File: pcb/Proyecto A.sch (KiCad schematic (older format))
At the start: 187 parts, among them J1 j, K1 1, K10 10, K11 k, K2 2, K3 3, K4 4, K6 6, K7 7, K8 8, K9 9, M1 KEYSW, P1 p, Q1 q, SW1 SW_Push, T1 t, U1 ATmega32U4-AU, U2 u, X1 x, Y1 16MHZ, Y2 y, k5 5

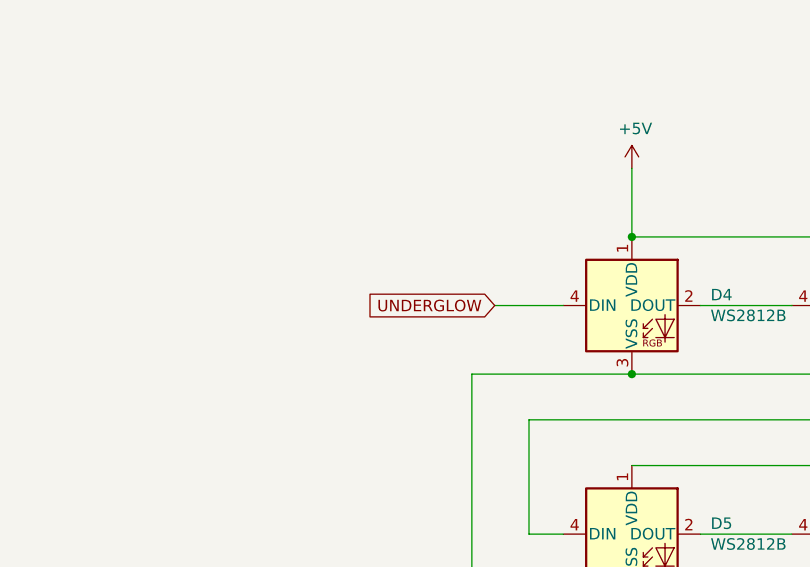
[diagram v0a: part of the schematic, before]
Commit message: added a 500 ohm resistor bettween mcu underglow pin and 1st ws2812b
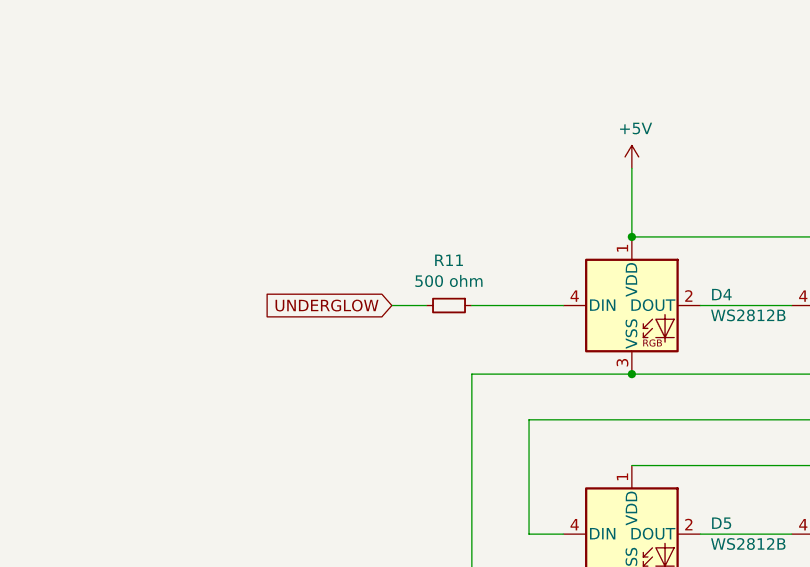
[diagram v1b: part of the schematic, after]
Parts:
- added R11: 500 ohm, Resistor_SMD:R_0805_2012Metric_Pad1.15x1.40mm_HandSolder, symbol Device:R_Small
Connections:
- net UNDERGLOW: now also R11.2; no longer D4.4 (DIN)
- new net: D4.4 (DIN), R11.1
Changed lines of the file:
@@
 Wire Wire Line
 	18600 8750 19000 8750
-Text GLabel 13700 7750 0    50   Input ~ 0
+Text GLabel 13250 7750 0    50   Input ~ 0
 UNDERGLOW
-Wire Wire Line
-	13700 7750 14000 7750
 NoConn ~ 19600 8750
 $Comp
@@
 Connection ~ 17300 11250
 Connection ~ 16350 10850
+$Comp
+L Device:R_Small R11
+U 1 1 5F167937
+P 13500 7750
+F 0 "R11" V 13304 7750 50  0000 C CNN
+F 1 "500 ohm" V 13395 7750 50  0000 C CNN
+F 2 "Resistor_SMD:R_0805_2012Metric_Pad1.15x1.40mm_HandSolder" H 13500 7750 50  0001 C CNN
+F 3 "~" H 13500 7750 50  0001 C CNN
+	1    13500 7750
+	0    1    1    0
+$EndComp
+Wire Wire Line
+	13250 7750 13400 7750
+Wire Wire Line
+	13600 7750 14000 7750
 $EndSCHEMATC

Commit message: Proto 1.1
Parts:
- '1, ,<1, .>1, /1, ;1, =+1, A1, ALT1, B1, B2, BACKSPACE1, C8, CAPS1, CAPS2, CTRL1, D18, E1, Esc1, F2, FUNC1, FUNC2, FUNCT1, G1, H1, I1, J1, K1, K10, K11, K2, K3, K4, K6, K7, K8, K9, KK0, K\1, K_14, L1, M1, N1, O1, P1, PGDN1, PGUP1, Q1, R10, RALT1, RCTL1, RETURN1, RSHIFT1, RSHIFT2, S1, SHIFT1, SPCE2, SPLIT_BKS1, T1, TAB1, U2, V1, W1, X1, Y2, Z1, [1, ]1, _-1, k5, lgui1, space2: symbol MX_Alps_Hybrid:MX-NoLED -> Proyecto-A-rescue:MX-NoLED-MX_Alps_Hybrid
- C1, C10, C11, C12, C13, C14, C15, C16, C17, C18, C19, C2, C20, C21, C3, C4, C5, C6, C9: footprint Capacitor_SMD:C_0805_2012Metric -> Capacitor_SMD:C_0805_2012Metric_Pad1.15x1.40mm_HandSolder
- C7: value 100uf -> 10uf; footprint Capacitor_SMD:C_0805_2012Metric -> Capacitor_SMD:C_0805_2012Metric_Pad1.15x1.40mm_HandSolder
- USB1: footprint Type-C:HRO-TYPE-C-31-M-12-jlc -> Type-C:HRO-TYPE-C-31-M-12-HandSoldering; symbol Type-C:HRO-TYPE-C-31-M-12 -> Proyecto-A-rescue:HRO-TYPE-C-31-M-12-Type-C
- Y1: footprint Crystal:Crystal_SMD_3225-4Pin_3.2x2.5mm -> Crystal:Crystal_SMD_3225-4Pin_3.2x2.5mm_HandSoldering
